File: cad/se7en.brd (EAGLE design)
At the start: 64 x 34 mm, 67 parts, among them CN1 MICROSD-EJECT, CN3 DO NOT PLACE, CN4 DO NOT PLACE, CN5 DO NOT PLACE, CN6 DO NOT PLACE, CN7 DO NOT PLACE, Q1 FDC6392S, SW1 SWITCHKMR211, SW2 SWITCHKMR211, U1 ATSAMS70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

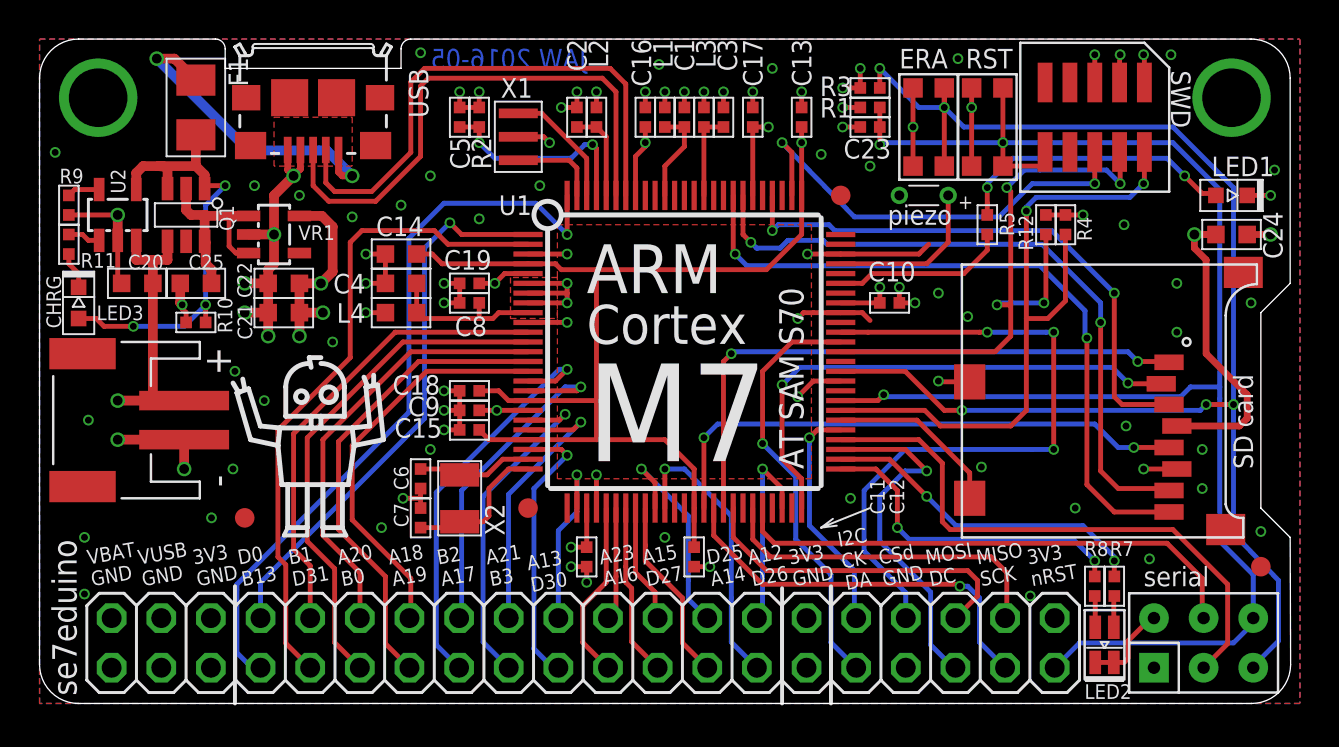
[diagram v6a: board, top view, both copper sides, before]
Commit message: move LEDs
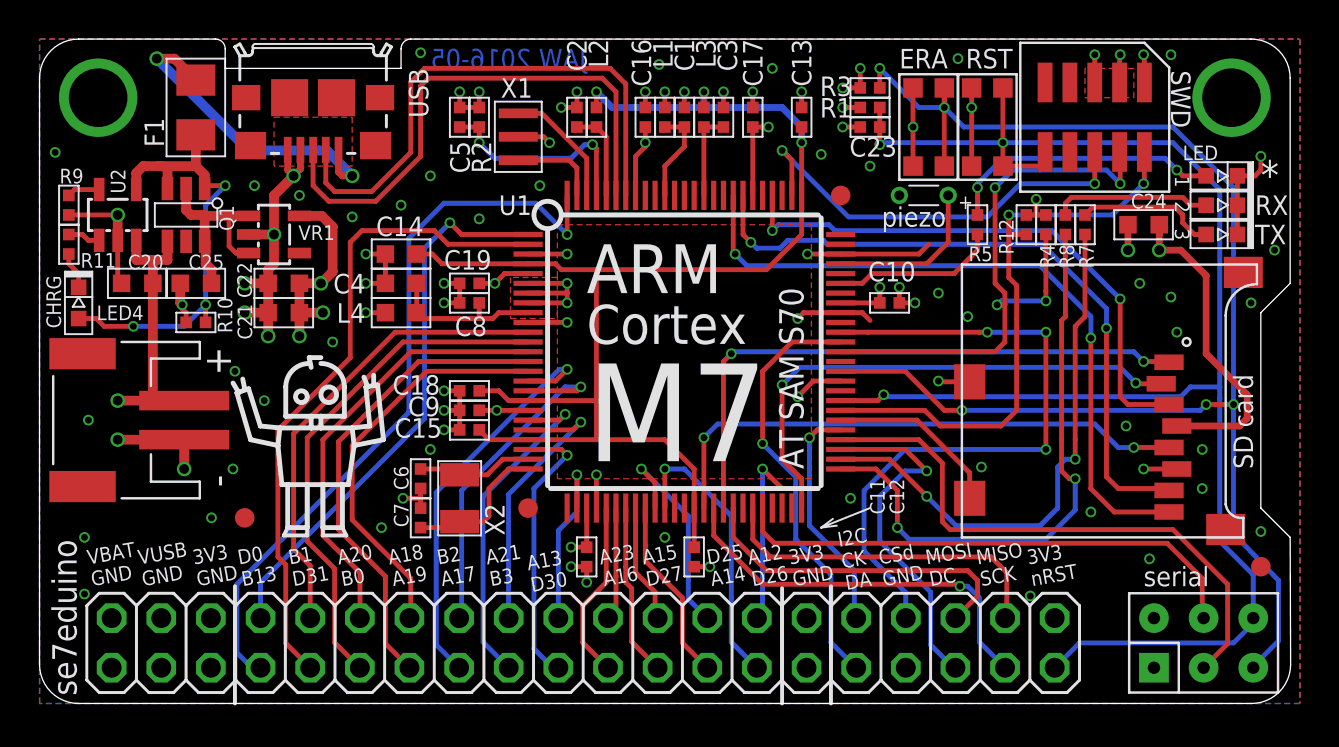
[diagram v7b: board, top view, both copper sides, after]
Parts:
- added LED4: RED, jaw:SMD0603D
- LED2: value LED-DUAL0805 -> green; device jaw:SMD0805-DUAL -> jaw:SMD0603D
- LED3: value RED -> orange
- moved LED3 58.6 mm to (116.5, 59.0), turned to 180 degrees
- moved LED2 23.3 mm to (116.5, 60.5), turned to 180 degrees
- moved R7 18.6 mm to (109.5, 59.5), turned to 270 degrees
- moved R8 18.6 mm to (108.5, 59.5), turned to 270 degrees
- moved C24 4.53 mm to (112.5, 59.5), turned to 0 degrees
- moved LED1 1.12 mm to (116.5, 62.0)
- moved R12 1.00 mm to (106.5, 59.5)
- moved R4 1.00 mm to (107.5, 59.5)
- moved R5 0.50 mm to (104.0, 59.5)
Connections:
- net GND: now also LED2.C, LED3.C; no longer LED2.2, LED2.3
- net N$12: now also LED4.C; no longer LED3.C
- net N$4: now also LED2.A; no longer LED2.1
- net N$5: now also LED3.A; no longer LED2.4
- net PINA12: no longer U1.48
- net SWCLK: now also R4.1; no longer R12.1
- net SWDIO: now also R12.1; no longer R4.1
- net VIN: now also LED4.A; no longer LED3.A
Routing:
- net IOLED2: track 16.9 -> 29.9 mm
- net IOLED3: track 17.1 -> 27.8 mm
- net N$4: track 1.61 -> 8.09 mm
- net N$5: track 1.60 -> 7.18 mm
- net SWDIO: track 34.5 -> 29.9 mm
- net PINA12: track 10.2 -> 9.16 mm
- net CSDPY: track 34.9 -> 34.1 mm
- net VCC: track 54.3 -> 55.0 mm
- net SWO: track 22.8 -> 22.2 mm
- net GND: track 100.4 -> 99.8 mm
- net IOLED1: track 9.00 -> 8.50 mm
- added copper zone on layer 1, net N$19
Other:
- board text added: "*"
- board text added: "1"
- board text added: "2"
- board text added: "3"
- board text added: "LED"
- board text added: "RX"
- board text added: "TX"

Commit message: piezo conn
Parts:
- removed CN6, CN7: DO NOT PLACE, jaw:HEADER-1X1-SMALL
- added CN8: HEADER-1X2-THM, jaw:HEADER-1X2-THM
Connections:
- net GND: now also CN8.P$2; no longer CN6.P$1
- net PIEZO: now also CN8.P$1; no longer CN7.P$1
- net PINA12: now also U1.48
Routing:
- net IOLED3: track 27.8 -> 25.3 mm
- net IOLED2: track 29.9 -> 28.4 mm
- net PINA12: track 9.16 -> 10.2 mm
- net SWO: track 22.2 -> 22.8 mm
- net GND: vias 92 -> 91
